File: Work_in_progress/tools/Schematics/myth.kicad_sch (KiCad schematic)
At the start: 125 parts, among them J1 Conn_01x08_Male, J2 Conn_01x08_Male, J3 Conn_01x08_Male, J4 Conn_01x08_Male, J5 Conn_01x04_Male, J6 Conn_01x04_Male, J7 Conn_02x01, U1 74AHC02, U10 74HC238, U11 74HC238, U12 74HC238, U13 4002, U14 74HC32, U15 74LS08, U16 74AHC273, U17 CD4532BE, U18 74AHC04, U19 74AHC138, U2 74AHC273, U20 74HC02, U21 74AHC02, U22 74HC238, U23 74HC238, U24 74LS08, U25 74AHC138, U26 4078, U27 74LS32, U28 74AHC138, U29 74AHC138, U3 74HC74, U30 4075, U31 74AHC244, U32 74AHC138, U33 74HC238, U34 74AHC138, U35 74HC163, U36 74AHC574, U37 74HC238, U38 74HC32, U39 74AHC04, U4 74AHC04, U40 74HC00, U41 74HC157, U42 74HC157, U43 74AHC574, U44 74LS21, U45 74AHC273, U46 74HC157, U47 74AHC04, U48 74AHC273, U49 74AHC244, U5 74AHC08, U50 74AHC04, U51 74AHC04, U52 74AHC273, U53 74HC283, U54 74HC283, U55 74AHC273, U56 74AHC244, U57 74AHC574, U58 27C080, U59 4078, U6 74HC595, U60 74HC74, U61 74HC193, U62 74HC193, U63 74HC193, U64 74HC193, U65 74AHC273, U66 74HC283, U67 74HC283, U68 74AHC244, U69 4078, U7 74HC165, U70 74AHC244, U71 74LS257, U72 74LS257, U73 74HC157, U74 74HC157, U75 74AHC244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

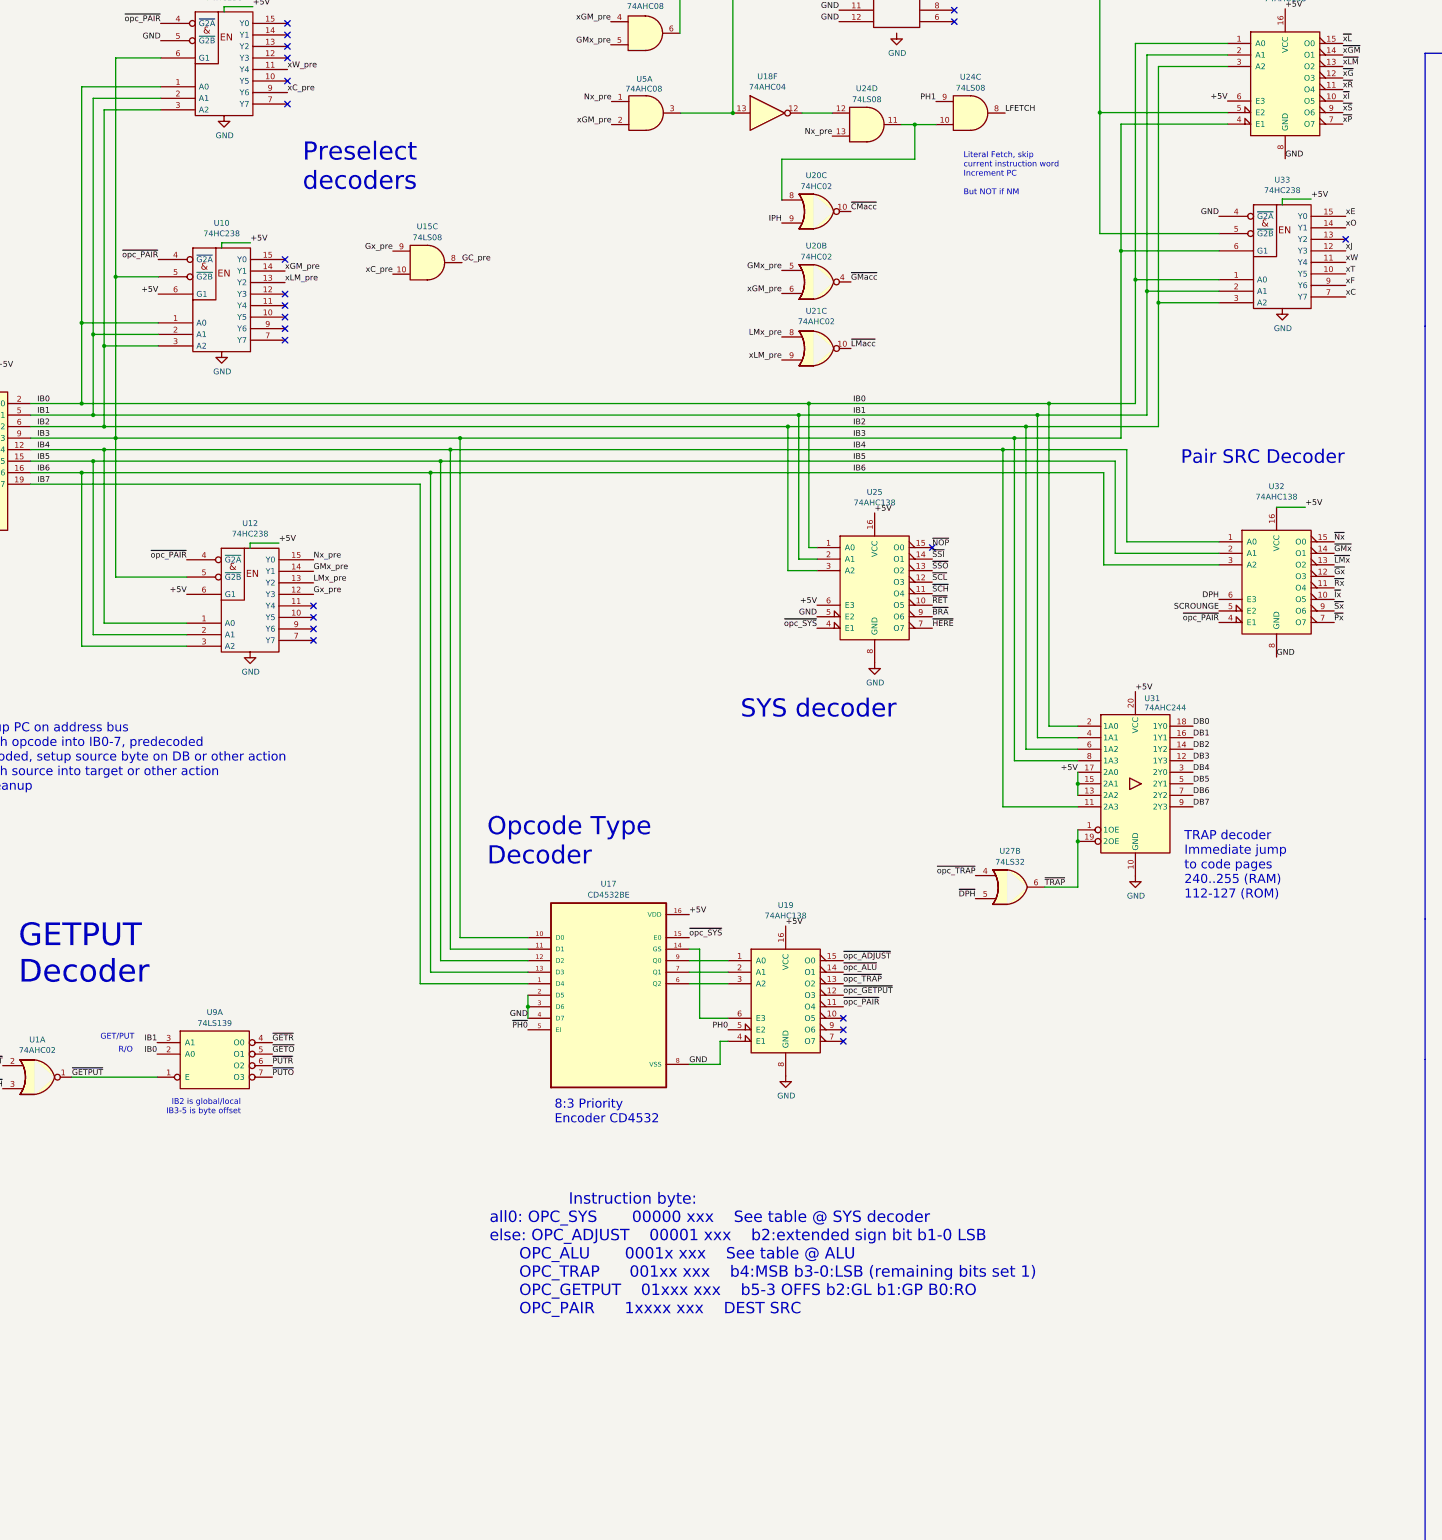
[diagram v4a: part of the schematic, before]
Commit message: Add B register
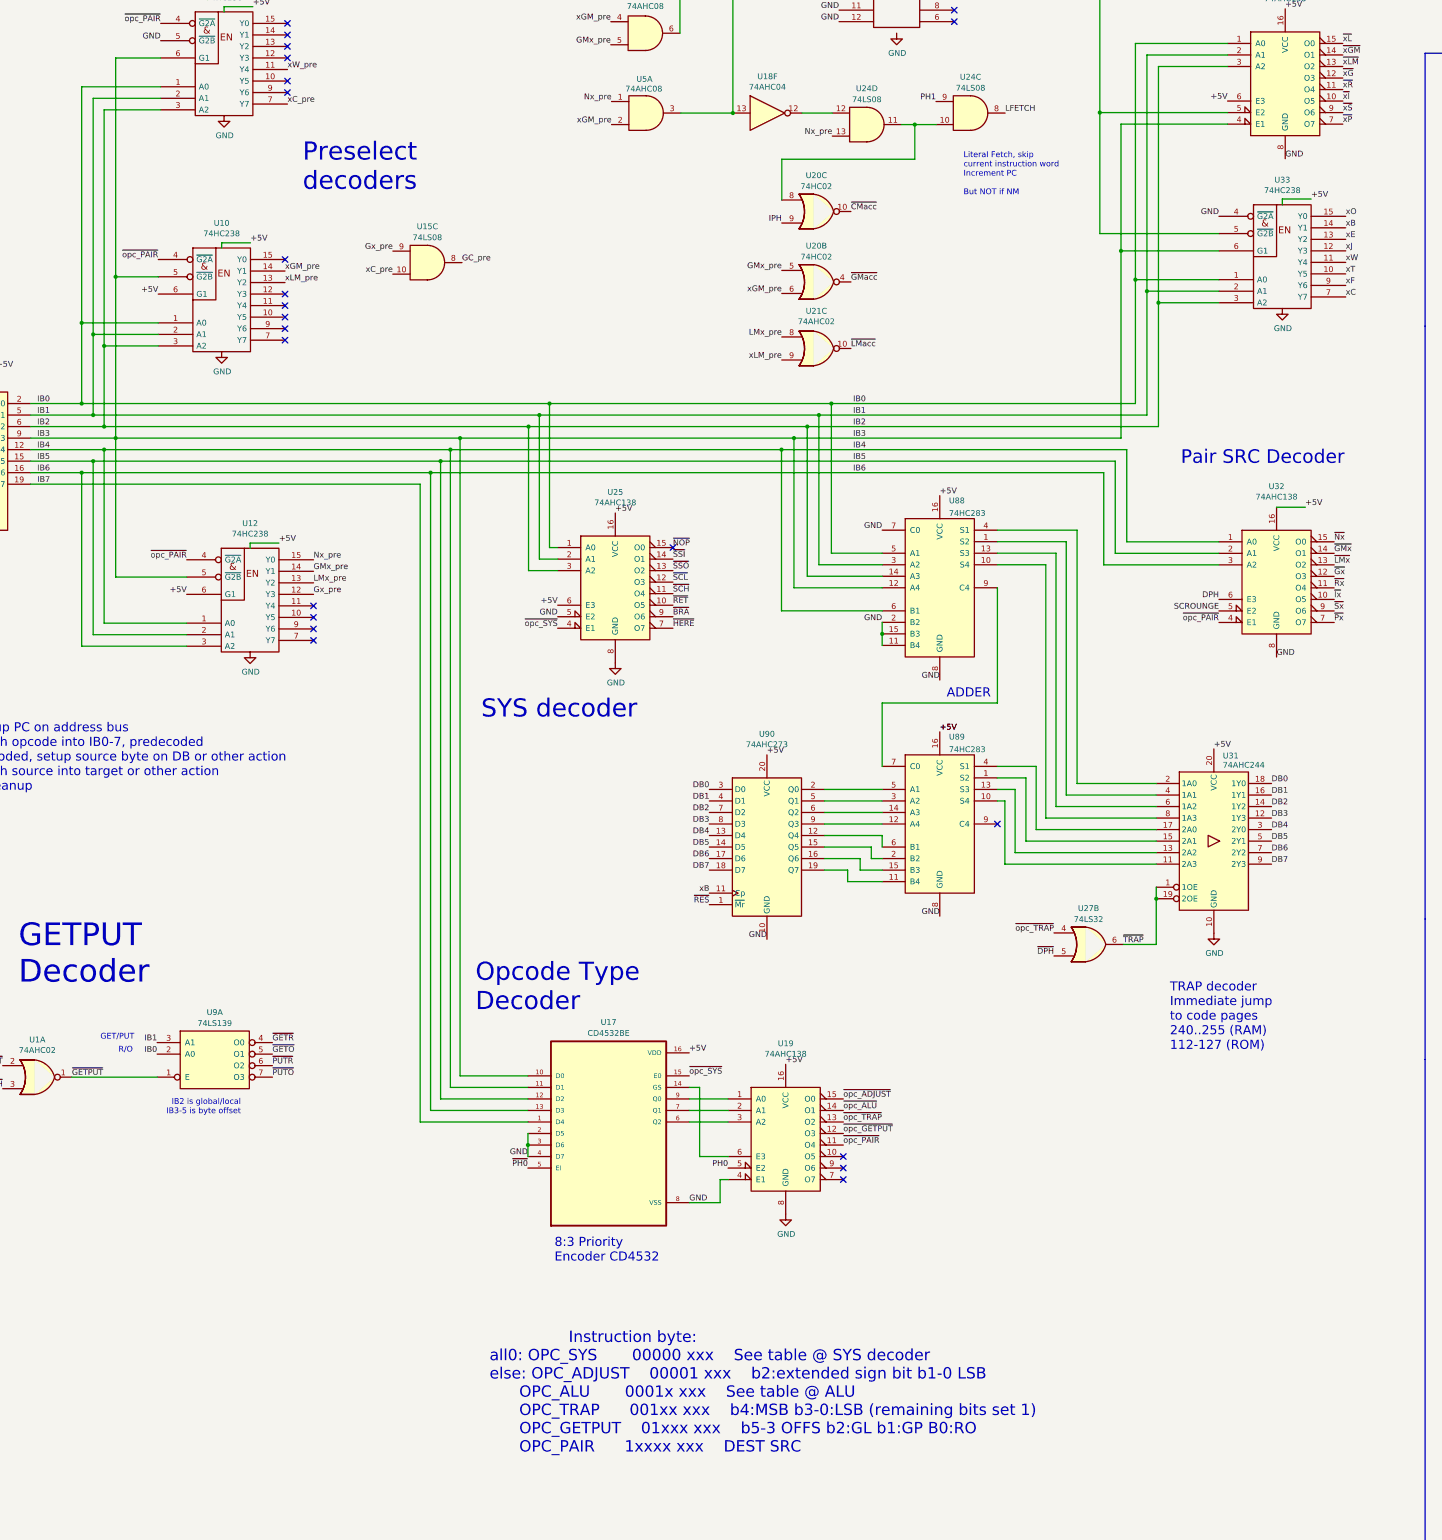
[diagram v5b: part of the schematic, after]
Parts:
- added U88, U89: 74HC283, Package_DIP:DIP-16_W7.62mm_Socket_LongPads, symbol 74xx:74LS283
- added U90: 74AHC273, Package_DIP:DIP-20_W7.62mm_Socket_LongPads, symbol 74xx:74HC273
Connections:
- net +5V: now also U88.16 (VCC), U89.16 (VCC), U90.20 (VCC); no longer U31.13 (2A2), U31.15 (2A1), U31.17 (2A0)
- net DB0: now also U90.3 (D0)
- net DB1: now also U90.4 (D1)
- net DB2: now also U90.7 (D2)
- net DB3: now also U90.8 (D3)
- net DB4: now also U90.13 (D4)
- net DB5: now also U90.14 (D5)
- net DB6: now also U90.17 (D6)
- net DB7: now also U90.18 (D7)
- net GND: now also U88.11 (B4), U88.15 (B3), U88.2 (B2), U88.7 (C0), U88.8 (GND), U89.8 (GND), U90.10 (GND)
- net IB0: now also U88.5 (A1); no longer U31.2 (1A0)
- net IB1: now also U88.3 (A2); no longer U31.4 (1A1)
- net IB2: now also U88.14 (A3); no longer U31.6 (1A2)
- net IB3: now also U88.12 (A4); no longer U31.8 (1A3)
- net IB4: now also U88.6 (B1); no longer U31.11 (2A3)
- net xC_pre: now also U11.7 (Y7); no longer U11.9 (Y6)
- net xE: now also U33.13 (Y2); no longer U33.15 (Y0)
- net xO: now also U33.15 (Y0); no longer U33.14 (Y1)
- net ~{RES}: now also U90.1 (~{Mr})
- new net: U89.6 (B1), U90.12 (Q4)
- new net: U89.2 (B2), U90.15 (Q5)
- new net: U89.15 (B3), U90.16 (Q6)
- new net: U89.11 (B4), U90.19 (Q7)
- new net: U89.5 (A1), U90.2 (Q0)
- new net: U89.3 (A2), U90.5 (Q1)
- new net: U89.14 (A3), U90.6 (Q2)
- new net: U89.12 (A4), U90.9 (Q3)
- new net: U31.4 (1A1), U88.1 (S2)
- new net: U31.8 (1A3), U88.10 (S4)
- new net: U31.6 (1A2), U88.13 (S3)
- new net: U31.2 (1A0), U88.4 (S1)
- new net: U88.9 (C4), U89.7 (C0)
- new net: U31.11 (2A3), U89.10 (S4)
- new net: U31.13 (2A2), U89.13 (S3)
- new net: U31.15 (2A1), U89.1 (S2)
- new net: U31.17 (2A0), U89.4 (S1)
- new net xB: U33.14 (Y1), U90.11 (Cp)
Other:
- moved on the sheet: U17, U19, U25, U27B, U31

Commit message: Fix bug in two adder instances
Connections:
- net DB0: now also U66.6 (B1); no longer U67.5 (A1)
- net DB1: now also U66.2 (B2); no longer U67.3 (A2)
- net DB2: now also U66.15 (B3); no longer U67.14 (A3)
- net DB3: now also U66.11 (B4); no longer U67.12 (A4)
- net GND: now also U89.12 (A4), U89.14 (A3), U89.3 (A2); no longer U88.11 (B4), U88.15 (B3), U88.2 (B2)
- net IB4: now also U89.5 (A1); no longer U88.6 (B1)
- net J4: now also U67.5 (A1); no longer U66.6 (B1)
- net J5: now also U67.3 (A2); no longer U66.2 (B2)
- net J6: now also U67.14 (A3); no longer U66.15 (B3)
- net J7: now also U67.12 (A4); no longer U66.11 (B4)
- net B4: now reaches U89.6 (B1), U90.12 (Q4)
- net B5: now reaches U89.2 (B2), U90.15 (Q5)
- net B6: now reaches U89.15 (B3), U90.16 (Q6)
- net B7: now reaches U89.11 (B4), U90.19 (Q7)
- net B0: now reaches U90.2 (Q0)
- net B0: now also U88.6 (B1); no longer U89.5 (A1)
- net B1: now reaches U90.5 (Q1)
- net B1: now also U88.2 (B2); no longer U89.3 (A2)
- net B2: now reaches U90.6 (Q2)
- net B2: now also U88.15 (B3); no longer U89.14 (A3)
- net B3: now reaches U90.9 (Q3)
- net B3: now also U88.11 (B4); no longer U89.12 (A4)

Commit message: Change design using xB(ase) xA(dd) pair
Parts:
- removed U70: 74AHC244, Package_DIP:DIP-20_W7.62mm_Socket_LongPads, symbol 74xx:74AHC244
- removed U88, U89: 74HC283, Package_DIP:DIP-16_W7.62mm_Socket_LongPads, symbol 74xx:74LS283
- removed U90: 74AHC273, Package_DIP:DIP-20_W7.62mm_Socket_LongPads, symbol 74xx:74HC273
- added U70, U88: 74HC157, Package_DIP:DIP-16_W7.62mm_Socket_LongPads, symbol 74xx:74LS157
- added U89: 74AHC273, Package_DIP:DIP-20_W7.62mm_Socket_LongPads, symbol 74xx:74HC273
- added U90, U91: 74HC283, Package_DIP:DIP-16_W7.62mm_Socket_LongPads, symbol 74xx:74LS283
- added U93: 74AHC244, Package_DIP:DIP-20_W7.62mm_Socket_LongPads, symbol 74xx:74AHC244
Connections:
- net +5V: now also U61.11 (~{LOAD}), U62.11 (~{LOAD}), U70.16 (VCC), U88.16 (VCC), U89.20 (VCC), U90.16 (VCC), U91.16 (VCC), U93.20 (VCC)
- net DB0: now also U70.2 (I0a), U90.5 (A1), U93.18 (1Y0); no longer U61.15 (A)
- net DB1: now also U70.5 (I0b), U90.3 (A2), U93.16 (1Y1); no longer U61.1 (B)
- net DB2: now also U70.11 (I0c), U90.14 (A3), U93.14 (1Y2); no longer U61.10 (C)
- net DB3: now also U70.14 (I0d), U90.12 (A4), U93.12 (1Y3); no longer U61.9 (D)
- net DB4: now also U88.2 (I0a), U91.5 (A1), U93.3 (2Y0); no longer U62.15 (A)
- net DB5: now also U88.5 (I0b), U91.3 (A2), U93.5 (2Y1); no longer U62.1 (B)
- net DB6: now also U88.11 (I0c), U91.14 (A3), U93.7 (2Y2); no longer U62.10 (C)
- net DB7: now also U88.14 (I0d), U91.12 (A4), U93.9 (2Y3); no longer U62.9 (D)
- net GND: now also U31.11 (2A3), U31.13 (2A2), U31.15 (2A1), U61.1 (B), U61.10 (C), U61.15 (A), U61.9 (D), U62.1 (B), U62.10 (C), U62.15 (A), U62.9 (D), U70.15 (E), U70.8 (GND), U88.15 (E), U88.8 (GND), U89.10 (GND), U90.7 (C0), U90.8 (GND), U91.8 (GND), U93.10 (GND); no longer U27.1, U27.2, U50.3
- net IB0: now also U31.2 (1A0)
- net IB1: now also U31.4 (1A1)
- net IB2: now also U31.6 (1A2)
- net IB3: now also U31.8 (1A3)
- net IB4: now also U31.17 (2A0)
- net xB: now also U27.2, U33.15 (Y0), U70.1 (S), U88.1 (S); no longer U33.14 (Y1)
- net xO: now also U50.4; no longer U33.15 (Y0)
- net ~{RES}: now also U89.1 (~{Mr})
- net at U27.3: now also U89.11 (Cp)
- net ~{Ix} renamed ~{Bx}
- net ~{Bx}: now also U93.1 (1OE), U93.19 (2OE)
- removed net ~{xL}: U34.15 (O0), U61.11 (~{LOAD}), U62.11 (~{LOAD})
- new net: U70.6 (I1b), U90.1 (S2)
- new net: U70.13 (I1d), U90.10 (S4)
- new net: U89.9 (Q3), U90.11 (B4), U93.8 (1A3)
- new net: U70.10 (I1c), U90.13 (S3)
- new net: U89.6 (Q2), U90.15 (B3), U93.6 (1A2)
- new net: U89.5 (Q1), U90.2 (B2), U93.4 (1A1)
- new net: U70.3 (I1a), U90.4 (S1)
- new net: U89.2 (Q0), U90.6 (B1), U93.2 (1A0)
- new net: U90.9 (C4), U91.7 (C0)
- new net: U89.12 (Q4), U91.6 (B1), U93.17 (2A0)
- new net: U89.15 (Q5), U91.2 (B2), U93.15 (2A1)
- new net: U89.16 (Q6), U91.15 (B3), U93.13 (2A2)
- new net: U89.19 (Q7), U91.11 (B4), U93.11 (2A3)
- new net: U88.6 (I1b), U91.1 (S2)
- new net: U88.13 (I1d), U91.10 (S4)
- new net: U88.10 (I1c), U91.13 (S3)
- new net: U88.3 (I1a), U91.4 (S1)
- new net Bin0: U70.4 (Za), U89.3 (D0)
- new net Bin1: U70.7 (Zb), U89.4 (D1)
- new net Bin2: U70.9 (Zc), U89.7 (D2)
- new net Bin3: U70.12 (Zd), U89.8 (D3)
- new net Bin4: U88.4 (Za), U89.13 (D4)
- new net Bin5: U88.7 (Zb), U89.14 (D5)
- new net Bin6: U88.9 (Zc), U89.17 (D6)
- new net Bin7: U88.12 (Zd), U89.18 (D7)
- new net xA: U27.1, U33.14 (Y1)
- new net ~{xO}: U34.15 (O0), U50.3
- no-connect marks 99 -> 97
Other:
- note added: "(BASE register)"
- note added: "(JUMP register) (Program Counter)"
- note added: "0 IDR ("Identity R" / R:=R) 1 IDO ("Identity O" / R:=Old) 2 OCR ("Ones Complement R" / R:=~R) 3 OCO ("Ones Complement O" / R:=~O) 4 SLR ("Shift left New" / R:=R<<1) 5 SLO ("Shift left Old" / R:=O<<1) 6 SRR ("Shift right R" / R:=R>>1) 7 SRO ("Shift right O" / R:=O>>1)"
- note added: "8 AND (R:=R&O) 9 IOR (R:=R|O) 10 EOR (R:=R^O) 11 ADD (Add" / R:=R+O, bits 0-7) 12 CAR ("Carry Bit" / R:= Carry, 9th bit of R+O) 00h or 01h 13 RLO ("Flag: R less than O" / R:= (R<O)? 0xFF:0 14 REO ("Flag: R equals O" / R:= (R==O)? 0xFF:0 15 RGO ("Flag: R greater than O" / R:= (R>O)? 0xFF:0"
- note added: "B"
- note added: "TRAP decoder Immediate calls"
- note added: "xB: set B xA: add to B"
- note removed: "(JUMP) register (Program Counter)"
- note removed: "0 IDN ("Identity New" / New:=New) 1 IDO ("Identity Old" / New:=Old) 2 OCR ("Ones Complement New" / New:=~New) 3 OCA ("Ones Complement Old" / New:=~Old) 4 SLR ("Shift left New" / New:=New<<1) 5 SLA ("Shift left Old" / New:=Old<<1) 6 SRR ("Shift right New" / New:=New>>1) 7 SRA ("Shift right Old" / New:=Old>>1)"
- note removed: "8 AND (New:=New&Old) 9 IOR (New:=New|Old) 10 EOR (New:=New^Old) 11 ADD (Add" / New:=New+Old, bits 0-7) 12 CAR ("Carry Bit" / New:= Carry, 9th bit of New+Old) 00h or 01h 13 NLO ("Flag: New less than Old" / New:= (New<Old)? 0xFF:0 14 NEO ("Flag: New equals Old" / New:= (New==Old)? 0xFF:0 15 NGO ("Flag: New greater than Old" / New:= (New>Old)? 0xFF:0"
- note removed: "BLUR3 LUT ROM"
- note removed: "TRAP decoder Immediate jump to code pages 240..255 (RAM) 112-127 (ROM)"
- moved on the sheet: U13B, U13C, U14A, U14B, U15A, U15E, U18A, U18B, U18C, U18D, U18E, U18G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

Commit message: WIP Edit single-stepper to reflect new KiCad model
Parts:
- removed unit 1 of U27
- removed U70, U88: 74HC157, Package_DIP:DIP-16_W7.62mm_Socket_LongPads, symbol 74xx:74LS157
- removed U89: 74AHC273, Package_DIP:DIP-20_W7.62mm_Socket_LongPads, symbol 74xx:74HC273
- removed U9: 74LS139, symbol 74xx:74LS139
- removed U90, U91: 74HC283, Package_DIP:DIP-16_W7.62mm_Socket_LongPads, symbol 74xx:74LS283
- removed U93: 74AHC244, Package_DIP:DIP-20_W7.62mm_Socket_LongPads, symbol 74xx:74AHC244
- added unit 1 of U23
- added U52, U91: 74LS32, symbol 74xx:74LS32
- added U53: 74AHC574, Package_DIP:DIP-20_W7.62mm_Socket_LongPads, symbol 74xx:74LS574
- added U65: 74AHC244, Package_DIP:DIP-20_W7.62mm_Socket_LongPads, symbol 74xx:74AHC244
- added U9: 74AHC138, Package_DIP:DIP-16_W7.62mm_Socket_LongPads, symbol 74xx:74LS138
- renumbered U6 to U10, U7 to U11, U8 to U12, U10 to U13, U11 to U14, U12 to U15, U13 to U16, U14 to U17, U16 to U18, U17 to U19, U25 to U20, U18 to U21, U19 to U22, U27 to U23, U22 to U24, U23 to U25, U31 to U27, U21 to U31, U43 to U41, U60 to U42, U76 to U43, U66 to U44, U67 to U45, U79 to U46, U20 to U47, U74 to U48, U73 to U49, U50 to U5, U82 to U50, U47 to U51, U61 to U55, U62 to U56, U80 to U57, U81 to U58, U63 to U59, U5 to U6, U64 to U60, U68 to U61, U69 to U62, U44 to U63, U51 to U64, U65 to U66, U77 to U67, U78 to U68, U41 to U69, U15 to U7, U42 to U70, U83 to U73, U45 to U74, U84 to U76, U46 to U77, U48 to U78, U49 to U79, U24 to U8, U87 to U80, U52 to U81, U53 to U82, U54 to U83, U55 to U84, U56 to U85, U57 to U86, U85 to U87, U86 to U88, U58 to U89, U59 to U90
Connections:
- net +5V: now also U63.9, U52.14 (VCC), U53.20 (VCC), U65.20 (VCC), U9.16 (VCC), U91.14 (VCC)
- net DB0: now also U53.19 (Q0), U53.2 (D0), U65.18 (1Y0)
- net DB1: now also U53.18 (Q1), U53.3 (D1), U65.16 (1Y1)
- net DB2: now also U53.17 (Q2), U53.4 (D2), U65.14 (1Y2)
- net DB3: now also U53.16 (Q3), U53.5 (D3), U65.12 (1Y3)
- net DB4: now also U53.15 (Q4), U53.6 (D4), U65.3 (2Y0)
- net DB5: now also U53.14 (Q5), U53.7 (D5), U65.5 (2Y1)
- net DB6: now also U53.13 (Q6), U53.8 (D6), U65.7 (2Y2)
- net DB7: now also U53.12 (Q7), U53.9 (D7), U65.9 (2Y3)
- net GETPUT: now also U1.1, U39.13, U40.10, U8.4, U52.10, U9.6 (E3); no longer U39.12
- net GND: now also U40.1, U40.2, U52.7 (GND), U53.10 (GND), U65.10 (GND), U9.4 (E1), U9.5 (E2), U9.8 (GND), U91.1, U91.12, U91.13, U91.2, U91.4, U91.5, U91.7 (GND); no longer U4.3, U4.9, U40.10, U40.9, U5.1, U5.13, U8.4, U8.5
- net I0: now also U65.2 (1A0)
- net I1: now also U65.4 (1A1)
- net I2: now also U65.6 (1A2)
- net I3: now also U65.8 (1A3)
- net I4: now also U65.17 (2A0)
- net I5: now also U65.15 (2A1)
- net I6: now also U65.13 (2A2)
- net I7: now also U65.11 (2A3)
- net IB0: now also U9.1 (A0)
- net IB1: now also U9.2 (A1)
- net IB2: now also U40.9, U5.1, U9.3 (A2)
- net LMx_pre: now also U52.4
- net xA: now also U33.15 (Y0), U23.2; no longer U33.14 (Y1)
- net xB: now also U33.14 (Y1); no longer U33.15 (Y0)
- net xLM_pre: now also U52.12
- net ~{GETO}: now also U9.14 (O1); no longer U40.1
- net ~{GETPUT}: now also U39.12; no longer U1.1, U39.13
- net ~{GETR}: now also U9.15 (O0); no longer U40.2
- net ~{LMacc}: now also U52.8; no longer U31.10
- net ~{PUTO}: now also U9.10 (O5); no longer U63.9
- net ~{PUTR}: now also U9.11 (O4); no longer U63.10
- net GETD: now reaches U4.8
- net GETD: now also U52.2
- net PUTD: now reaches U4.4
- net PUTD: now also U91.9
- net GETA: now reaches U5.12
- net GETA: now also U23.1
- net GET: now reaches U8.6
- net GET: now also U16.9
- net Nx_pre_clean: now reaches U47.8, U8.10, U8.11
- net ~{PUT}: now reaches U40.8
- net ~{PUT}: now also U63.10
- net at U40.3: no longer U16.9
- net at U5.2: now also U8.5
- net G0 renamed D0
- net G1 renamed D1
- net G2 renamed D2
- net G3 renamed D3
- net G4 renamed D4
- net G5 renamed D5
- net G6 renamed D6
- net G7 renamed D7
- net GC_pre renamed DC_pre
- net GMx renamed DMx
- net GMx_pre renamed DMx_pre
- net DMx_pre: now also U52.5; no longer U6.5
- net Gx: no longer names the net of U31.12
- net Gx: now also U91.8; no longer U5.8
- net Gx_pre renamed Dx_pre
- net HERE renamed ORG
- net ORG: now also U30.2
- net xG renamed intoD
- net intoD: now also U30.8, U52.3; no longer U21.10, U30.2
- net xGM_pre renamed xDM_pre
- net xDM_pre: now also U52.13; no longer U6.2, U6.4
- net ~{Bx} renamed ~{Ix}
- net ~{Ix}: now also U65.1 (1OE), U65.19 (2OE)
- net ~{GMacc} renamed ~{DMacc}
- net ~{GMx} renamed ~{DMx}
- net ~{Gx} renamed ~{Dx}
- net ~{HERE} renamed ~{ORG}
- net ~{ORG}: no longer U30.8
- net ~{xGM} renamed ~{xDM}
- net ~{xG} renamed ~{xD}
- new net: U52.6, U6.4
- new net: U52.11, U6.2, U6.5
- new net: U31.10, U52.9
- new net: U23.3, U53.11 (Cp)
- new net Dx: U5.8, U91.10
- new net xD: U21.10, U52.1
- new net ~{GETA}: U5.13, U9.12 (O3)
- new net ~{GETD}: U4.9, U9.13 (O2)
- new net ~{PUTA}: U53.1 (OE), U9.7 (O7)
- new net ~{PUTD}: U4.3, U9.9 (O6)
- no-connect marks 97 -> 91
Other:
- note added: "(A spare register)"
- note added: "(DATA) Page index"
- note added: "A"
- note added: "Anything"
- note added: "Broadcast"
- note added: "D"
- note added: "IB3-5 is byte offset"
- note added: "Mx"
- note added: "Prevent same-cycle memory-to-memory copy"
- note added: "R/O/G/A"
- note added: "xM"
- note removed: "(BASE register)"
- note removed: "(GLOBAL) Page index"
- note removed: "B"
- note removed: "G"
- note removed: "IB2 is global/local IB3-5 is byte offset"
- note removed: "R/O"
- note removed: "xB: set B xA: add to B"
- moved on the sheet: U1A, U31C, U40A, U40C, U47B, U47C, U4D, U5A, U5F, U7C, U7D, U8B
